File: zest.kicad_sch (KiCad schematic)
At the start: 7 parts

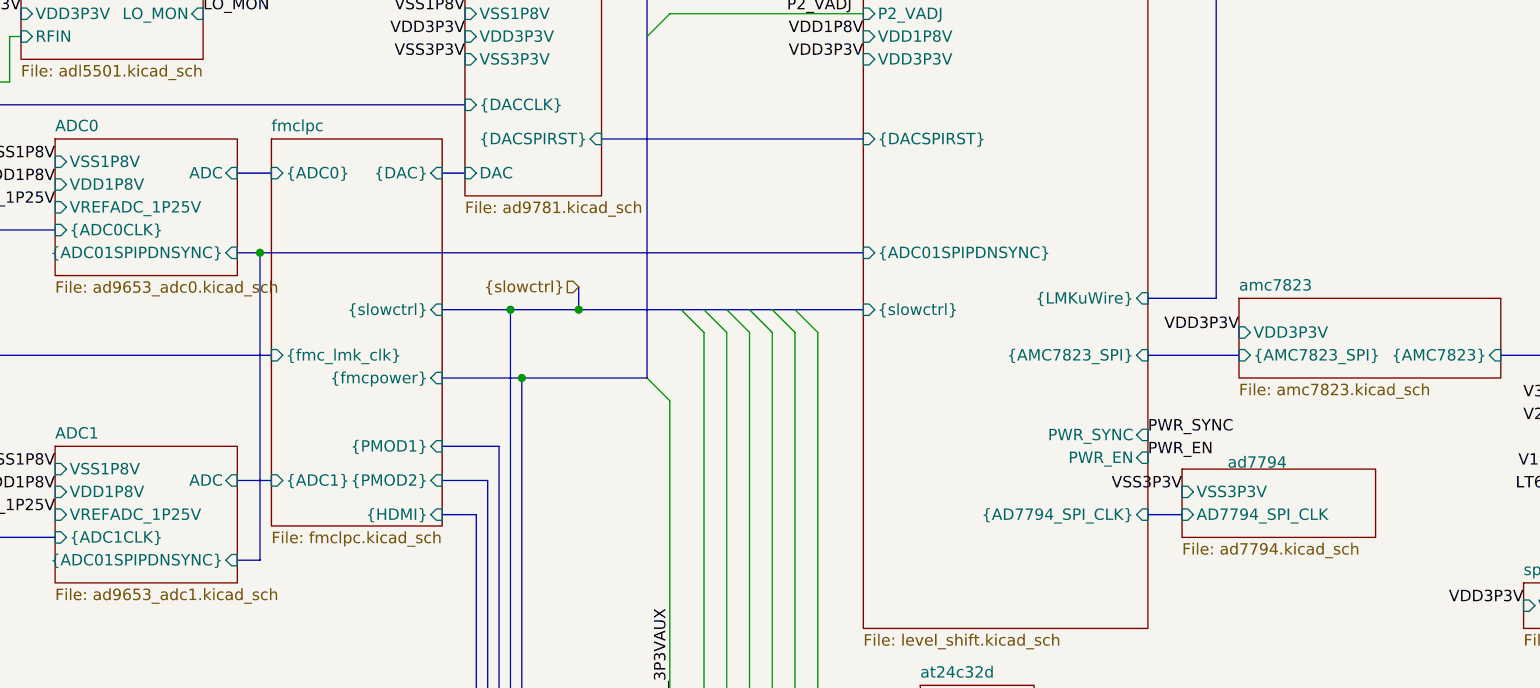
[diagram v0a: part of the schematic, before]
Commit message: Updates from Michal to fix ERC errors
Still lots of ERC warnings
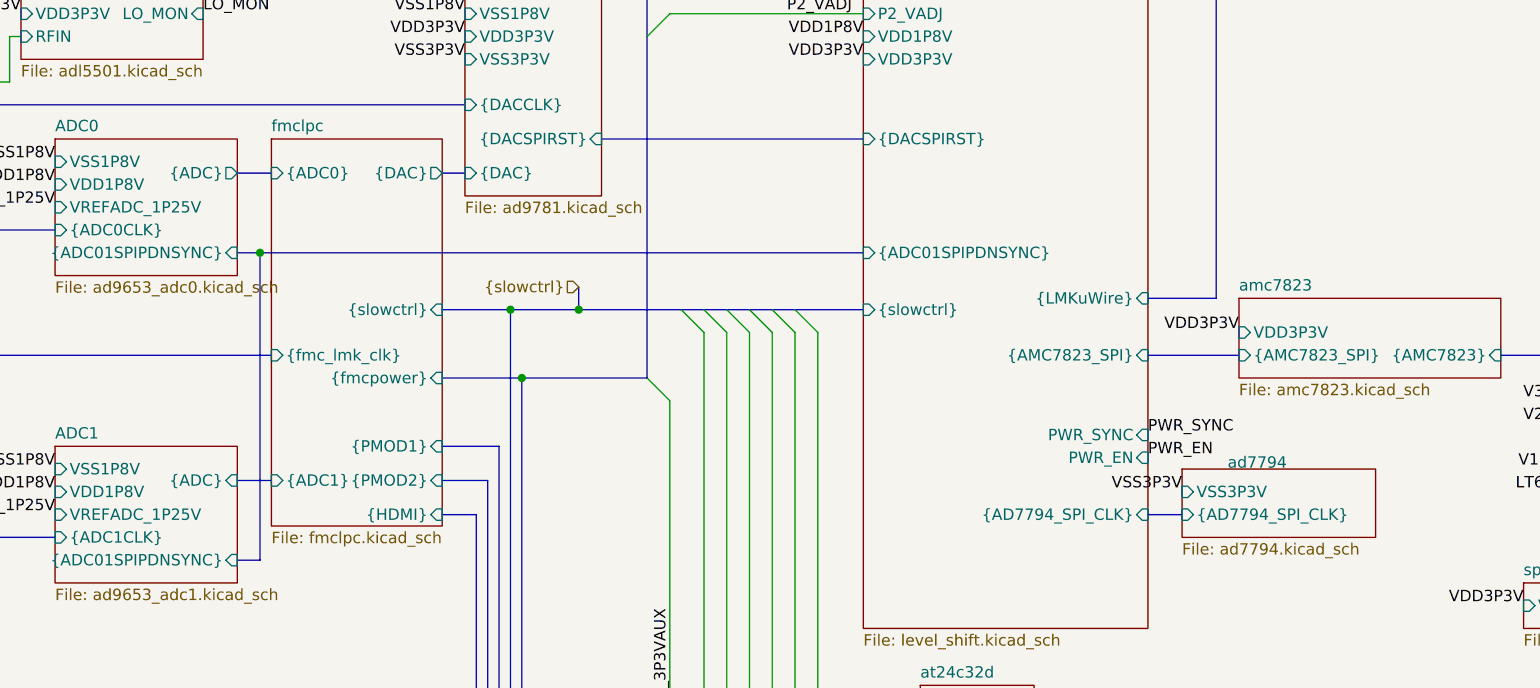
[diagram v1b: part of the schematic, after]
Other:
- sheet ADC0 ports: added {ADC}; removed ADC
- sheet ADC1 ports: added {ADC}; removed ADC
- sheet ad7794 ports: added {AD7794_SPI_CLK}; removed AD7794_SPI_CLK
- sheet ad9781 ports: added {DAC}; removed DAC
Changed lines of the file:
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@@
 			)
 		)
-		(pin "ADC" input
+		(pin "{ADC}" output
 			(at 81.28 74.93 0)
 			(effects
@@
 			)
 		)
-		(pin "ADC" input
+		(pin "{ADC}" input
 			(at 81.28 109.22 0)
 			(effects
@@
 			)
 		)
-		(pin "AD7794_SPI_CLK" input
+		(pin "{AD7794_SPI_CLK}" input
 			(at 186.69 113.03 180)
 			(effects
@@
 			)
 		)
-		(pin "DAC" input
+		(pin "{DAC}" input
 			(at 106.68 74.93 180)
 			(effects
@@
 			)
 		)
-		(pin "{DAC}" input
+		(pin "{DAC}" output
 			(at 104.14 74.93 0)
 			(effects

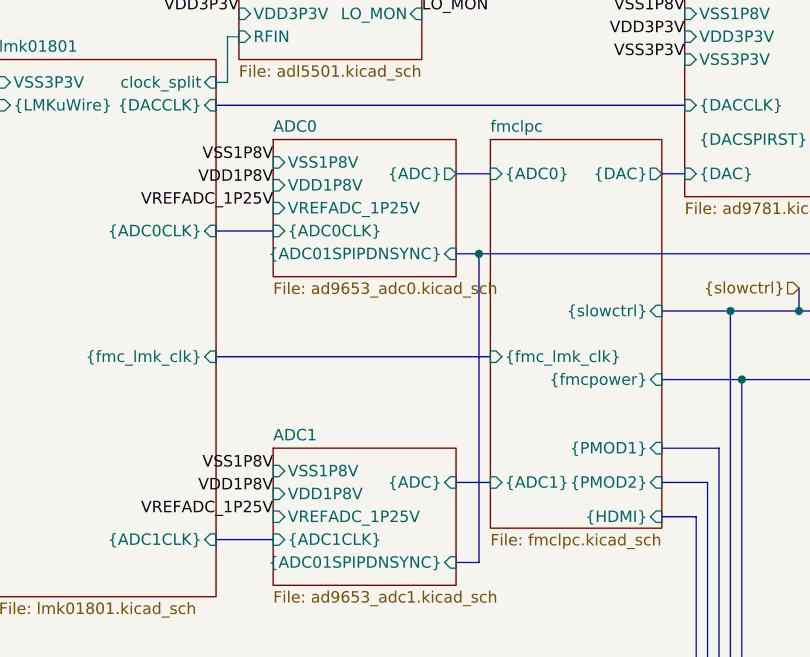
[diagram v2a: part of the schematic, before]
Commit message: Updated some Schematics
- updated slowmon schematic
- updated diff to se schematic
- cleaned up DRC/ERC errors
No changes were made that effected the PCB layout
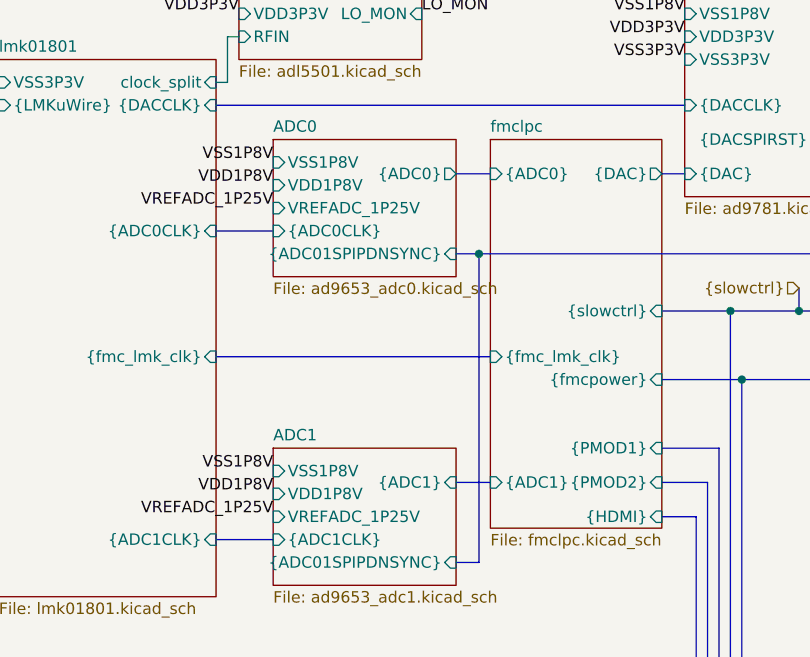
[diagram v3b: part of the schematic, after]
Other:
- sheet ADC0 ports: added {ADC0}; removed {ADC}
- sheet ADC1 ports: added {ADC1}; removed {ADC}
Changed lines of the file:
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@@
 			)
 		)
-		(pin "{ADC}" output
+		(pin "{ADC0}" output
 			(at 81.28 74.93 0)
 			(effects
@@
 			)
 		)
-		(pin "{ADC}" input
+		(pin "{ADC1}" input
 			(at 81.28 109.22 0)
 			(effects
